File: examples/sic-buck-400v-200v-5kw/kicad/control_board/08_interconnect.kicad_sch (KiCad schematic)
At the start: 30 parts, among them J8 J_MEZZ: 2 x 25 header to the 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

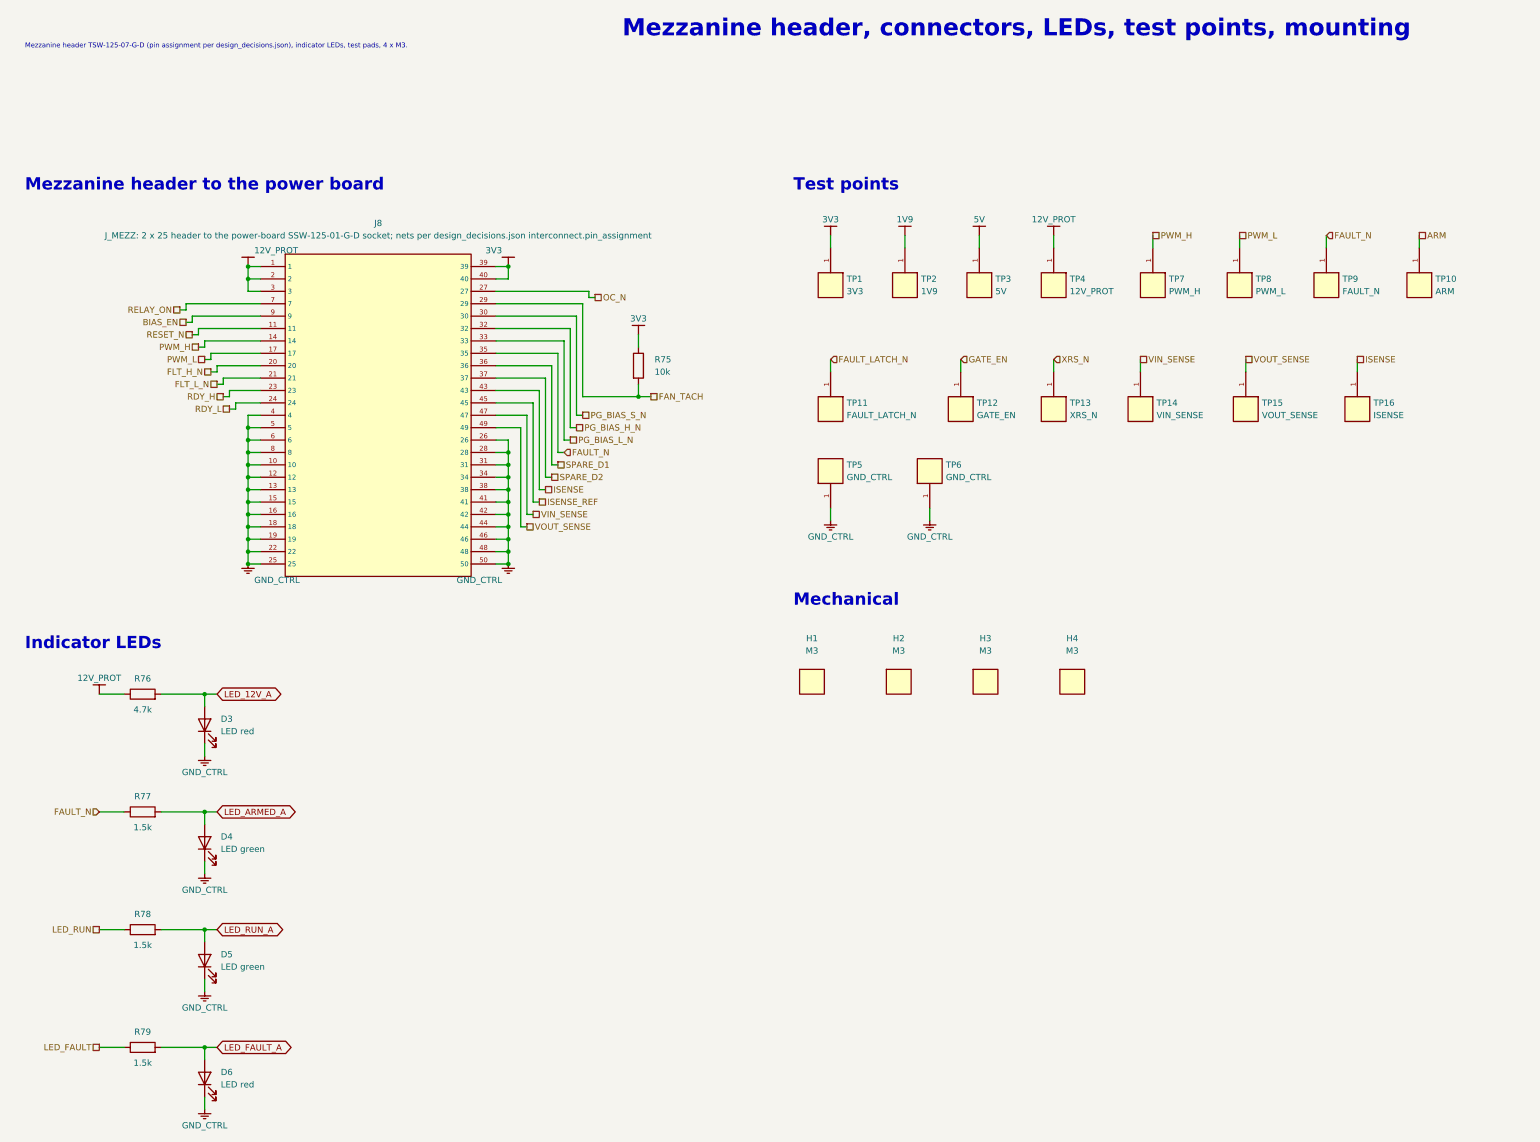
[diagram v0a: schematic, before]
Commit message: Correct sensing circuits and add verified V2.2 local bypasses
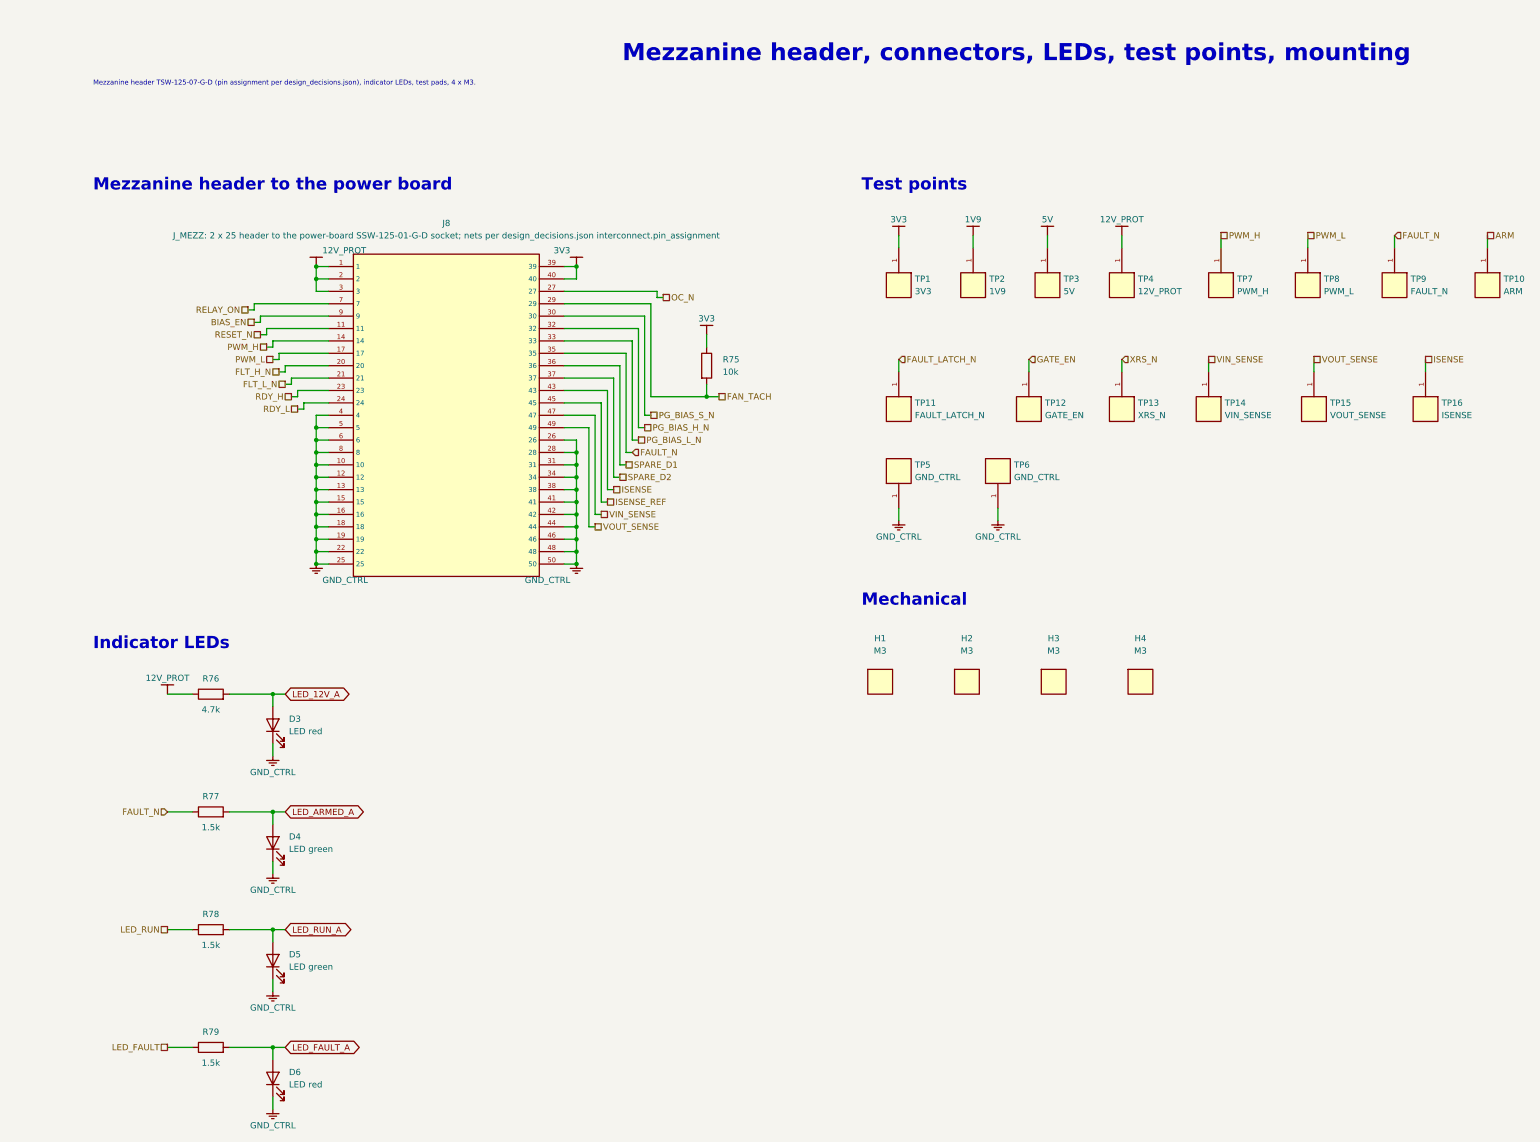
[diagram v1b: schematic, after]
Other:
- moved on the sheet: D3, D4, D5, D6, H1, H2, H3, H4, J8, R75, R76, R77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
